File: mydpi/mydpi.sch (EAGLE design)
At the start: 29 parts, among them Q1 DMN3404L, U1 MEGA32U4-MU, U2 AP7381-33Y-13

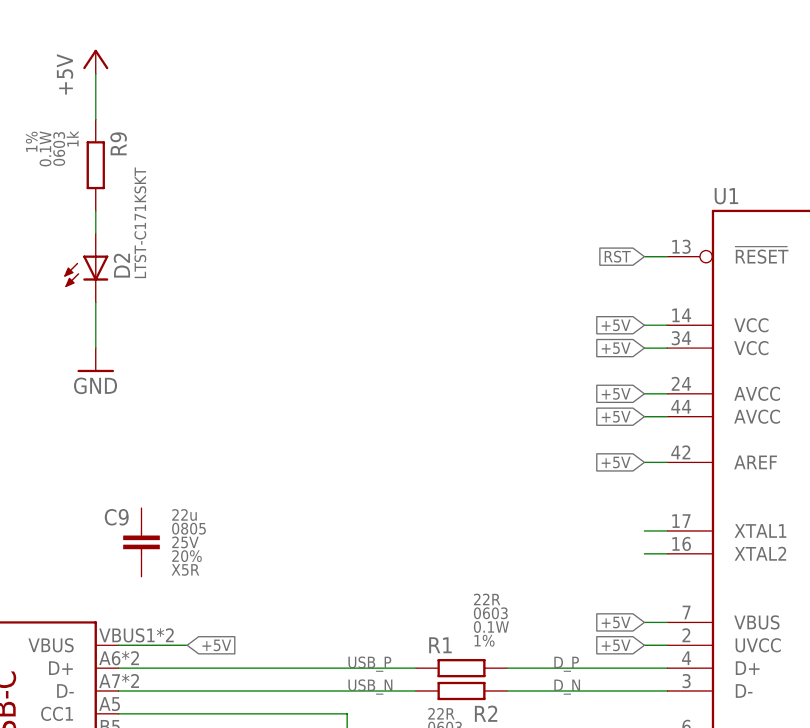
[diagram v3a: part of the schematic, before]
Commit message: Crystal Added
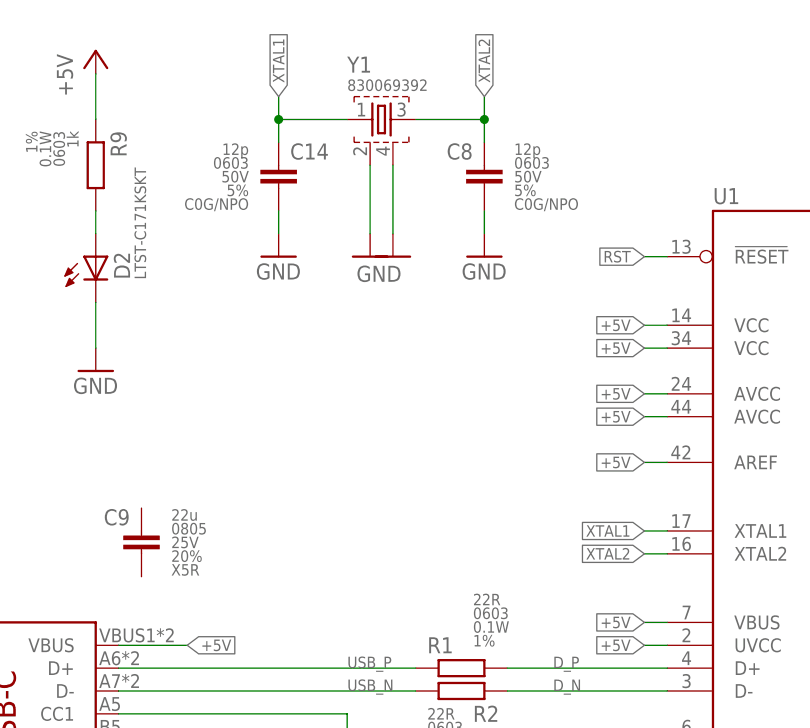
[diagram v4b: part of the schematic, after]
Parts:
- added C14, C8: 12p, zaan-Capacitors:12PF-0603-50V-5%
- added Y1: 830069392, zaan-Electromechanical:830069392
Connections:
- removed net N$13: U1.XTAL1
- removed net N$14: U1.XTAL2
- new net XTAL1: C14.1, U1.XTAL1, Y1.1
- new net XTAL2: C8.1, U1.XTAL2, Y1.3
- net GND: now also C14.2, C8.2, Y1.2, Y1.4
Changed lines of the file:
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@@
 <part name="P+2" library="supply1" library_urn="urn:adsk.eagle:library:371" deviceset="+5V" device=""/>
 <part name="GND17" library="supply1" library_urn="urn:adsk.eagle:library:371" deviceset="GND" device=""/>
+<part name="C8" library="zaan-Capacitors" deviceset="12PF" device="-0603-50V-5%" package3d_urn="urn:adsk.eagle:package:23616/2" value="12p"/>
+<part name="C14" library="zaan-Capacitors" deviceset="12PF" device="-0603-50V-5%" package3d_urn="urn:adsk.eagle:package:23616/2" value="12p"/>
+<part name="Y1" library="zaan-Electromechanical" deviceset="830069" device="392" package3d_urn="urn:adsk.eagle:package:13029088/2"/>
+<part name="GND16" library="supply1" library_urn="urn:adsk.eagle:library:371" deviceset="GND" device=""/>
+<part name="GND18" library="supply1" library_urn="urn:adsk.eagle:library:371" deviceset="GND" device=""/>
+<part name="GND19" library="supply1" library_urn="urn:adsk.eagle:library:371" deviceset="GND" device=""/>
+<part name="GND20" library="supply1" library_urn="urn:adsk.eagle:library:371" deviceset="GND" device=""/>
 </parts>
 <sheets>
@@
 <instance part="GND17" gate="1" x="35.56" y="205.74" smashed="yes">
 <attribute name="VALUE" x="33.02" y="203.2" size="1.778" layer="96"/>
+</instance>
+<instance part="C8" gate="G$1" x="78.74" y="228.6" smashed="yes">
+<attribute name="NAME" x="77.47" y="230.124" size="1.778" layer="95" rot="R180" align="center-left"/>
+<attribute name="VALUE" x="82.042" y="230.378" size="1.27" layer="96" align="center-left"/>
+<attribute name="PACKAGE-IN" x="82.042" y="228.854" size="1.27" layer="96" align="center-left"/>
+<attribute name="VOLTAGE" x="82.042" y="227.33" size="1.27" layer="96" align="center-left"/>
+<attribute name="TOLERANCE" x="82.042" y="225.806" size="1.27" layer="96" align="center-left"/>
+<attribute name="DIELECTRIC" x="82.042" y="224.282" size="1.27" layer="96" align="center-left"/>
+</instance>
+<instance part="C14" gate="G$1" x="55.88" y="228.6" smashed="yes" rot="MR0">
+<attribute name="NAME" x="57.15" y="230.124" size="1.778" layer="95" rot="MR180" align="center-left"/>
+<attribute name="VALUE" x="52.578" y="230.378" size="1.27" layer="96" rot="MR0" align="center-left"/>
+<attribute name="PACKAGE-IN" x="52.578" y="228.854" size="1.27" layer="96" rot="MR0" align="center-left"/>
+<attribute name="VOLTAGE" x="52.578" y="227.33" size="1.27" layer="96" rot="MR0" align="center-left"/>
+<attribute name="TOLERANCE" x="52.578" y="225.806" size="1.27" layer="96" rot="MR0" align="center-left"/>
+<attribute name="DIELECTRIC" x="52.578" y="224.282" size="1.27" layer="96" rot="MR0" align="center-left"/>
+</instance>
+<instance part="Y1" gate="G$1" x="66.04" y="233.68" smashed="yes">
+<attribute name="NAME" x="63.5" y="239.776" size="1.778" layer="95" align="center-left"/>
+<attribute name="VALUE" x="63.5" y="237.49" size="1.27" layer="96" align="center-left"/>
+</instance>
+<instance part="GND16" gate="1" x="66.04" y="218.44" smashed="yes"/>
+<instance part="GND18" gate="1" x="68.58" y="218.44" smashed="yes">
+<attribute name="VALUE" x="64.516" y="215.646" size="1.778" layer="96"/>
+</instance>
+<instance part="GND19" gate="1" x="55.88" y="218.44" smashed="yes">
+<attribute name="VALUE" x="53.34" y="215.9" size="1.778" layer="96"/>
+</instance>
+<instance part="GND20" gate="1" x="78.74" y="218.44" smashed="yes">
+<attribute name="VALUE" x="76.2" y="215.9" size="1.778" layer="96"/>
 </instance>
 </instances>
@@
 <pinref part="GND17" gate="1" pin="GND"/>
 </segment>
+<segment>
+<pinref part="Y1" gate="G$1" pin="2"/>
+<wire x1="66.04" y1="228.6" x2="66.04" y2="220.98" width="0.1524" layer="91"/>
+<pinref part="GND16" gate="1" pin="GND"/>
+</segment>
+<segment>
+<pinref part="Y1" gate="G$1" pin="4"/>
+<wire x1="68.58" y1="228.6" x2="68.58" y2="220.98" width="0.1524" layer="91"/>
+<pinref part="GND18" gate="1" pin="GND"/>
+</segment>
+<segment>
+<pinref part="GND19" gate="1" pin="GND"/>
+<pinref part="C14" gate="G$1" pin="2"/>
+<wire x1="55.88" y1="220.98" x2="55.88" y2="223.52" width="0.1524" layer="91"/>
+</segment>
+<segment>
+<pinref part="GND20" gate="1" pin="GND"/>
+<pinref part="C8" gate="G$1" pin="2"/>
+<wire x1="78.74" y1="220.98" x2="78.74" y2="223.52" width="0.1524" layer="91"/>
+</segment>
 </net>
 <net name="N$1" class="0">
@@
 </segment>
 </net>
-<net name="N$13" class="0">
-<segment>
-<pinref part="U1" gate="G$1" pin="XTAL1"/>
-<wire x1="99.06" y1="187.96" x2="96.52" y2="187.96" width="0.1524" layer="91"/>
-</segment>
-</net>
-<net name="N$14" class="0">
-<segment>
-<pinref part="U1" gate="G$1" pin="XTAL2"/>
-<wire x1="99.06" y1="185.42" x2="96.52" y2="185.42" width="0.1524" layer="91"/>
-</segment>
-</net>
 <net name="D_P" class="0">
 <segment>
@@
 </segment>
 </net>
+<net name="XTAL1" class="0">
+<segment>
+<pinref part="C14" gate="G$1" pin="1"/>
+<wire x1="55.88" y1="231.14" x2="55.88" y2="233.68" width="0.1524" layer="91"/>
+<pinref part="Y1" gate="G$1" pin="1"/>
+<wire x1="55.88" y1="233.68" x2="63.5" y2="233.68" width="0.1524" layer="91"/>
+<wire x1="55.88" y1="233.68" x2="55.88" y2="236.22" width="0.1524" layer="91"/>
+<junction x="55.88" y="233.68"/>
+<label x="55.88" y="236.22" size="1.27" layer="95" rot="R90" xref="yes"/>
+</segment>
+<segment>
+<pinref part="U1" gate="G$1" pin="XTAL1"/>
+<wire x1="99.06" y1="187.96" x2="96.52" y2="187.96" width="0.1524" layer="91"/>
+<label x="96.52" y="187.96" size="1.27" layer="95" rot="R180" xref="yes"/>
+</segment>
+</net>
+<net name="XTAL2" class="0">
+<segment>
+<pinref part="C8" gate="G$1" pin="1"/>
+<wire x1="78.74" y1="231.14" x2="78.74" y2="233.68" width="0.1524" layer="91"/>
+<pinref part="Y1" gate="G$1" pin="3"/>
+<wire x1="78.74" y1="233.68" x2="71.12" y2="233.68" width="0.1524" layer="91"/>
+<wire x1="78.74" y1="233.68" x2="78.74" y2="236.22" width="0.1524" layer="91"/>
+<junction x="78.74" y="233.68"/>
+<label x="78.74" y="236.22" size="1.27" layer="95" rot="R90" xref="yes"/>
+</segment>
+<segment>
+<pinref part="U1" gate="G$1" pin="XTAL2"/>
+<wire x1="99.06" y1="185.42" x2="96.52" y2="185.42" width="0.1524" layer="91"/>
+<label x="96.52" y="185.42" size="1.27" layer="95" rot="R180" xref="yes"/>
+</segment>
+</net>

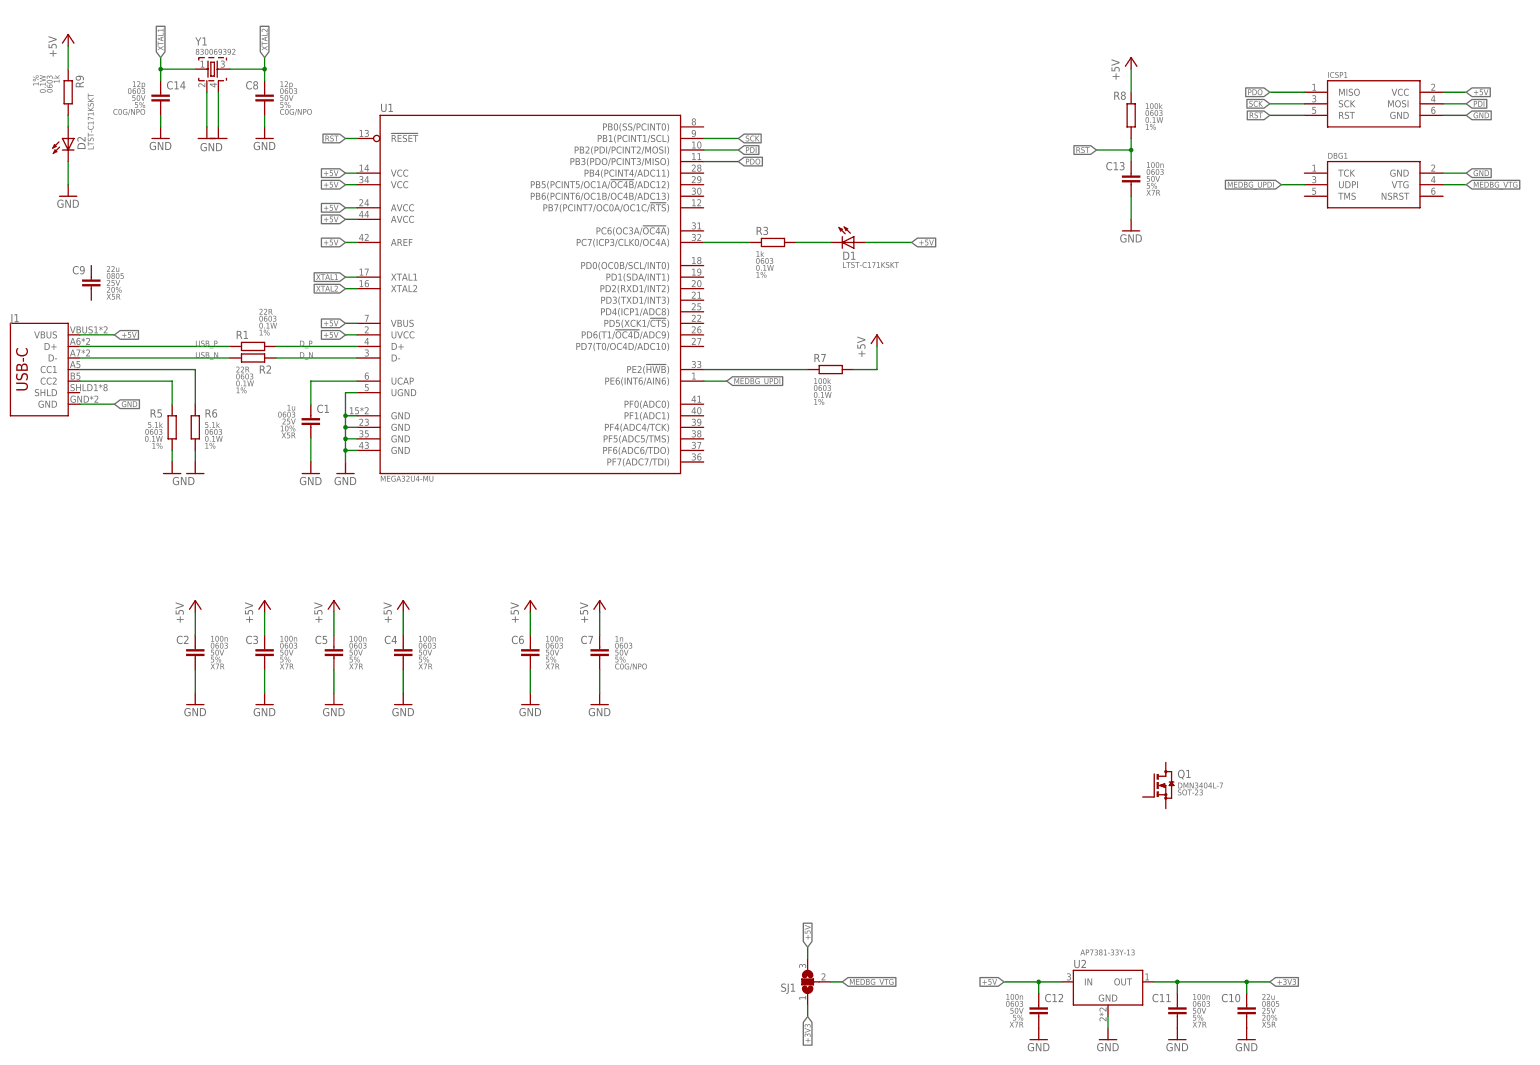
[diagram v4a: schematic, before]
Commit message: Added Reset Switch
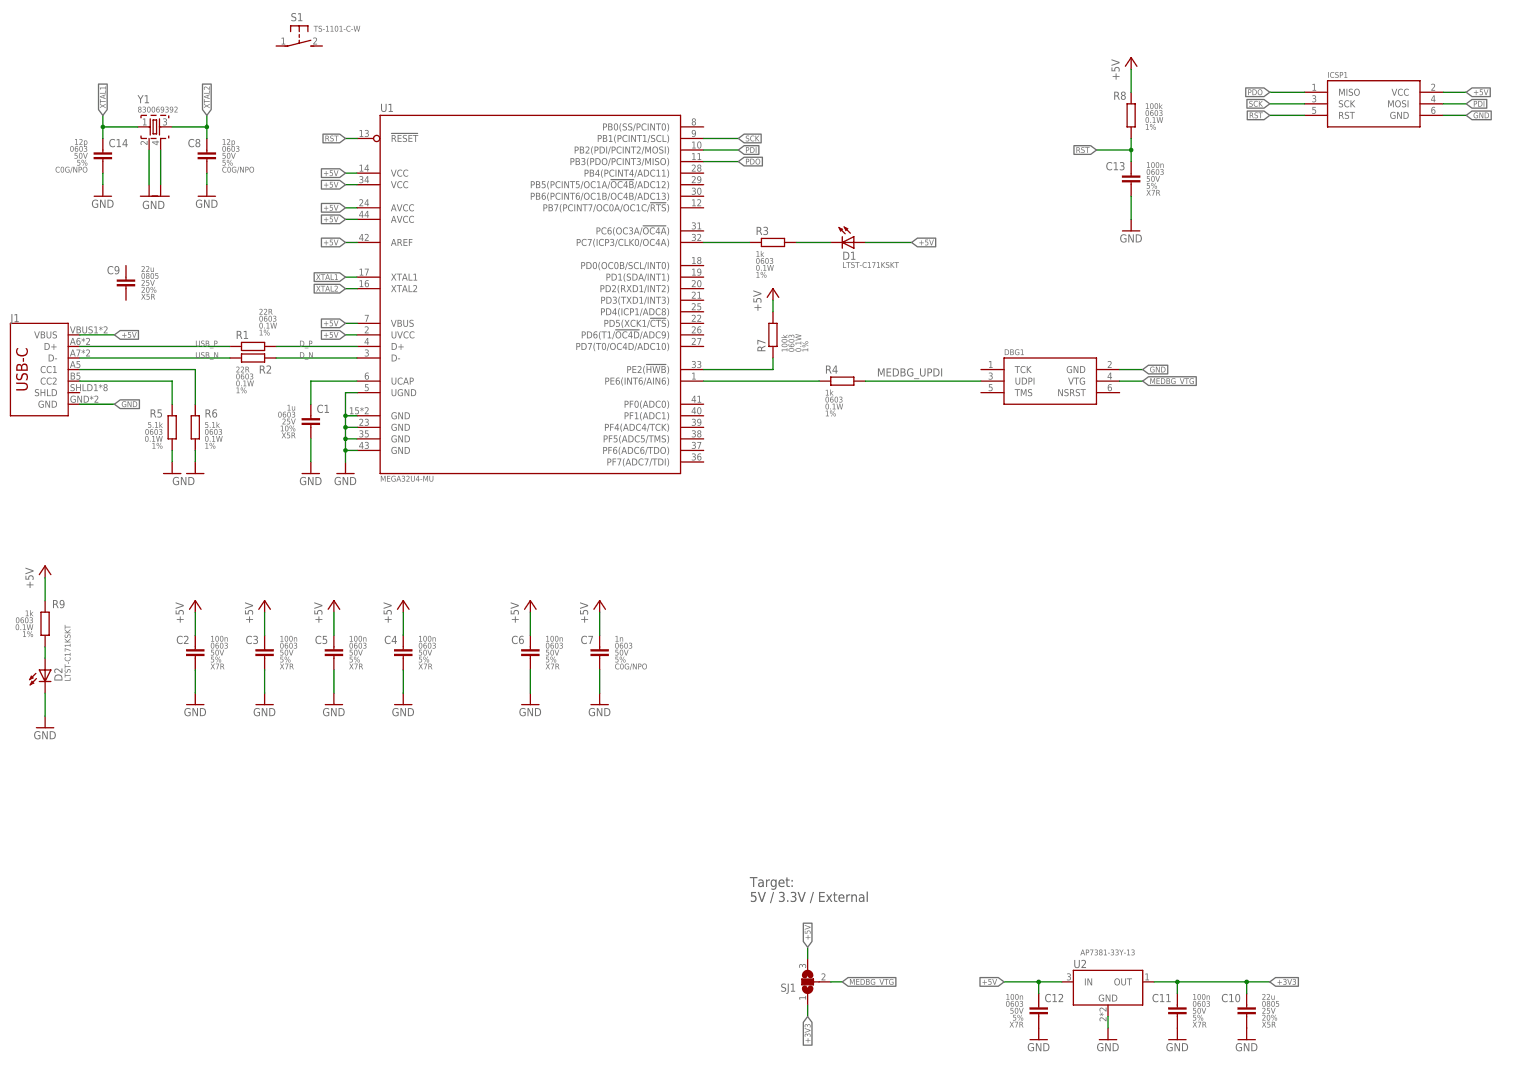
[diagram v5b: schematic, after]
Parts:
- removed Q1: DMN3404L, zaan-Discrete:DMN3404L
- added R4: 1k, zaan-Resistors:1KOHM-0603-1/10W-1%
- added S1: TS-1101-C-W, zaan-Electromechanical:TS-1101-C-W
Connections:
- new net PE6: R4.1, U1.PE6(INT6/AIN6)
- net MEDBG_UPDI: now also R4.2; no longer U1.PE6(INT6/AIN6)
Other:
- note added: "Target: 5V / 3.3V / External"
- moved on the sheet: C14, C8, C9, D2, DBG1, R7, R9, Y1

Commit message: Button and Fuse added
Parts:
- added F1: 0ZCF0050FF2C, zaan-Fuses:0ZCF0050FF2C
- DBG1: value AVR-UPDI-SKEDD -> AVR-UPDI-6-SKEDD; device zaan-Connectors:AVR-UPDI-SKEDD -> zaan-Connectors:AVR-UPDI-6-SKEDD
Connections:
- net GND: now also S1.P
- net RST: now also S1.S
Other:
- moved on the sheet: C13, R8, S1
